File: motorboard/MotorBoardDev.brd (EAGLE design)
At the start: 86 x 80.5 mm, 70 parts, among them J1 Under Glow, J2 B2PS-VH(LF)(SN), J3 B2PS-VH(LF)(SN), J4 B2PS-VH(LF)(SN), Q1 SSM3J338R, Q2 SSM3J338R, Q3 SSM3J338R, Q4 STT4P3LLH6, U1 TXB0104DR, U2 9DoF IMU, U3 TXB0106PWR, U4 TLV70233DBVR, X1 C-GRID-05-15-91, X2 C-GRID-05-15-91, X3 MINI-USB_SHIELD5P4-32005-400, X4 C-GRID-02-70553, X5 SI-50170, X7 2510-, X8 2510-

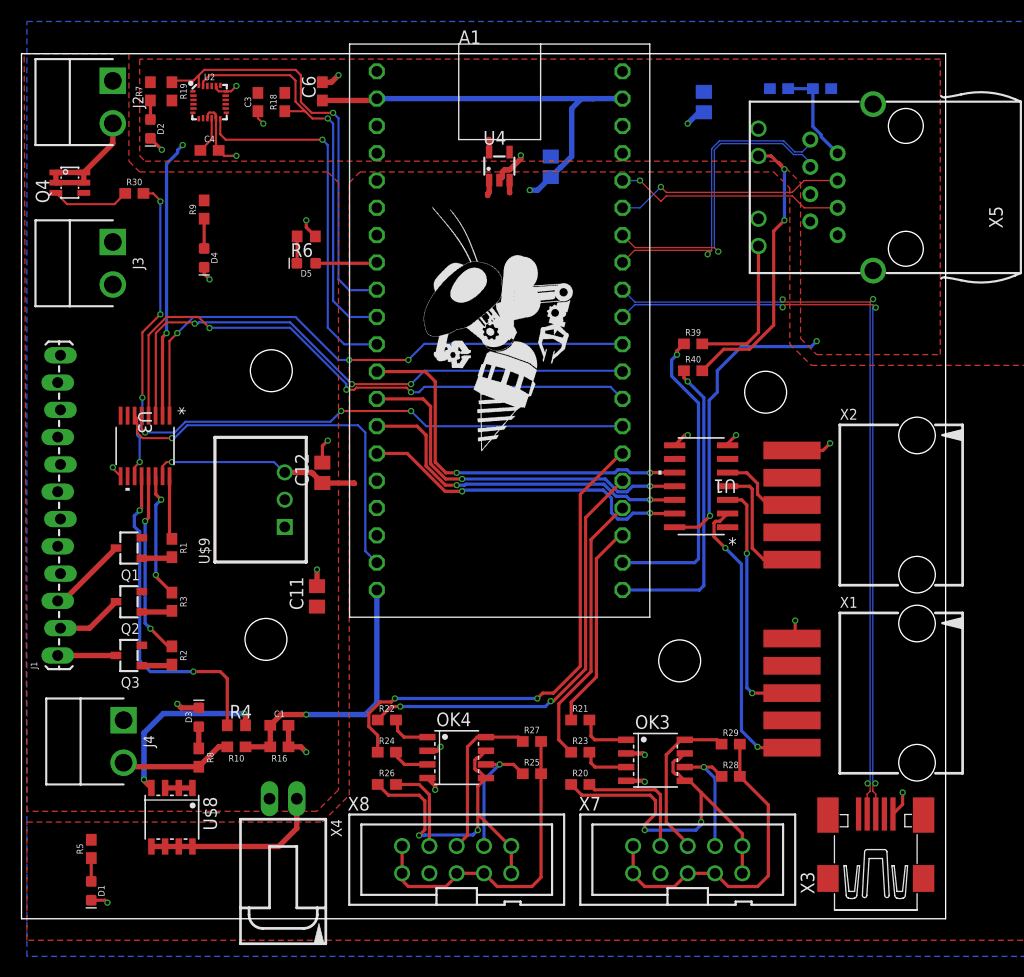
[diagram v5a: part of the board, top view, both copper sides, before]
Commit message: Differential and Silkscreen fixed
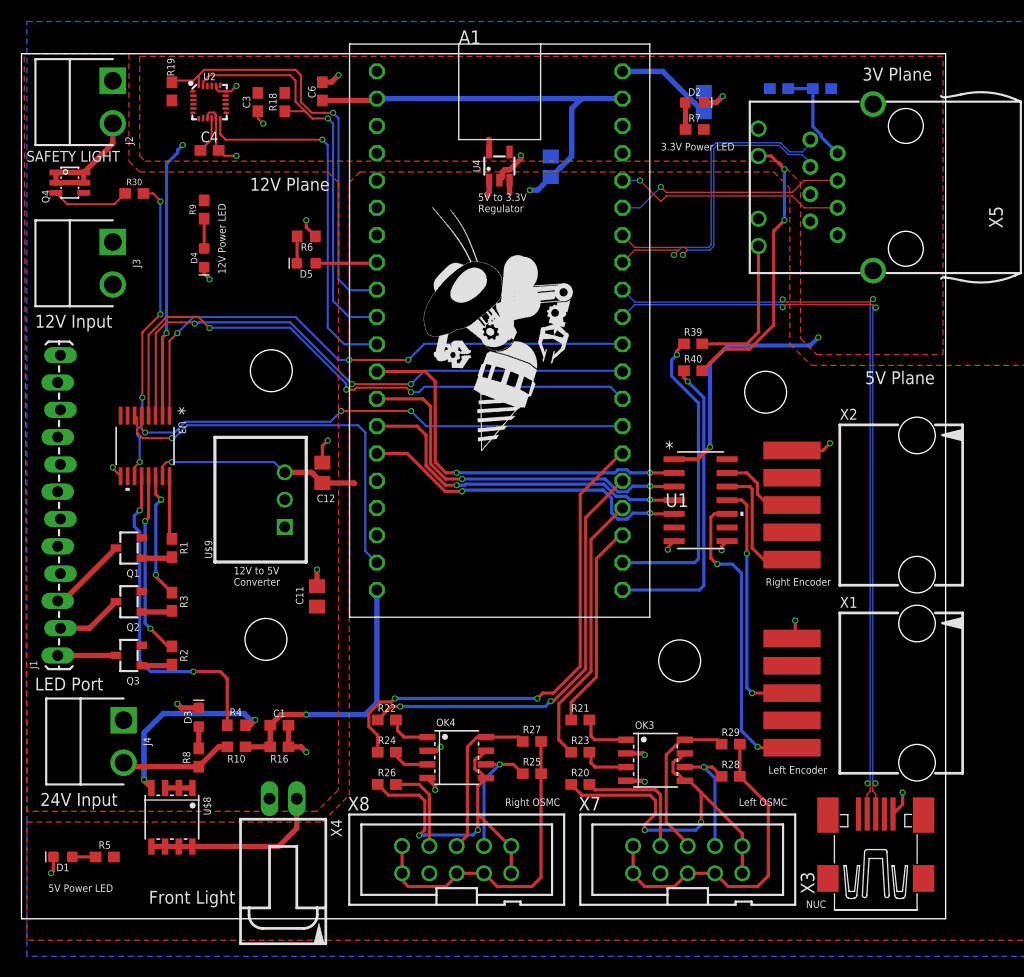
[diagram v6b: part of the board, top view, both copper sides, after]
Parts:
- moved R7 50.8 mm to (70.2, 73.5), turned to 0 degrees
- moved D2 50.7 mm to (70.2, 76.0), turned to 0 degrees
- moved D1 4.12 mm to (11.3, 5.76), turned to 180 degrees
- moved R5 1.46 mm to (15.2, 5.75), turned to 0 degrees
- moved U1 1.30 mm to (70.7, 39.0), turned to 0 degrees
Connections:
- net N$1 renamed SAFETY_HRD
- net N$10 renamed FRONT_HDR
- net N$12 renamed 12V_LED_R
- net N$17 renamed MBED_R_LED1
- net N$18 renamed MBED_R_LED2
- net N$19 renamed GREEN_R
- net N$2 renamed REGOUT_C
- net N$26 renamed RED_R
- net N$29 renamed R_OK3A
- net N$3 renamed INDI_LED_R
- net N$30 renamed R_OK4A
- net N$31 renamed R_OK4B
- net N$32 renamed R_OK3B
- net N$4 renamed BLUE_R
- net N$5 renamed 5V_LED_R
- net N$6 renamed 3V3_LED_R
- net N$7 renamed SAFETY_R
- net N$8 renamed FRONT_R
- net N$9 renamed 24V_LED_R
- net +3V3: now also U1.1; no longer U1.14
- net +5V: now also U1.14; no longer U1.1
- net LEA: now also U1.11; no longer U1.3
- net LEA3: now also U1.4; no longer U1.12
- net LEB: now also U1.10; no longer U1.2
- net LEB3: now also U1.5; no longer U1.13
- net REA: now also U1.13; no longer U1.5
- net REA3: now also U1.2; no longer U1.10
- net REB: now also U1.12; no longer U1.4
- net REB3: now also U1.3; no longer U1.11
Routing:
- net +3V3: track 66.3 -> 68.2 mm, vias 5 -> 4
- net LEB: track 27.4 -> 28.9 mm
- net FRONT_R: track 16.6 -> 17.9 mm
- net +5V: track 62.5 -> 61.4 mm
- net 3V3_LED_R: track 1.77 -> 2.51 mm
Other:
- board text added: "12V Input"
- board text added: "12V Plane"
- board text added: "12V Power LED"
- board text added: "12V to 5V Converter"
- board text added: "24V Input"
- board text added: "3.3V Power LED"
- board text added: "3V Plane"
- board text added: "5V Plane"
- board text added: "5V Power LED"
- board text added: "5V to 3.3V Regulator"
- board text added: "Front Light"
- board text added: "LED Port"
- board text added: "Left Encoder"
- board text added: "Left OSMC"
- board text added: "NUC"
- board text added: "Right Encoder"
- board text added: "Right OSMC"
- board text added: "SAFETY LIGHT"

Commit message: moved board
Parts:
- moved D2 7.50 mm to (62.6, 76.0)
- moved R7 7.50 mm to (62.6, 73.5)
- moved A1 7.50 mm to (44.5, 56.0)
- moved C1 7.50 mm to (24.0, 18.0)
- moved C11 7.50 mm to (27.5, 30.0)
- moved C12 7.50 mm to (28.0, 41.5)
- moved C13 7.50 mm to (49.3, 70.0)
- moved C14 7.50 mm to (63.5, 76.0)
- moved C2 7.50 mm to (74.5, 77.2)
- moved C3 7.50 mm to (22.0, 76.0)
- moved C4 7.50 mm to (17.5, 71.5)
- moved C5 7.50 mm to (70.5, 77.2)
- moved C6 7.50 mm to (28.0, 77.0)
- moved D1 7.50 mm to (3.85, 5.76)
- moved D3 7.50 mm to (16.5, 18.8)
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
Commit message: changed front light to flood light
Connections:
- net RD+ renamed RD_P
- net RD- renamed RD_N
- net GND: now also U3.8
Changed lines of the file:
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@@
 <wire x1="64.65" y1="75.95" x2="65.25" y2="76.55" width="0.5" layer="1"/>
 <via x="65.25" y="76.55" extent="1-16" drill="0.35"/>
+<contactref element="U3" pad="8"/>
+<wire x1="75.35" y1="77.25" x2="79.25" y2="75.812" width="0" layer="19" extent="16-16"/>
+<wire x1="69.65" y1="77.25" x2="75.35" y2="77.25" width="0" layer="19" extent="16-16"/>
+<wire x1="68.582" y1="73.526" x2="69.65" y2="77.25" width="0" layer="19" extent="16-16"/>
+<wire x1="65.25" y1="76.55" x2="69.65" y2="77.25" width="0" layer="19" extent="16-16"/>
+<wire x1="63.5" y1="76.95" x2="63.527" y2="75.95" width="0" layer="19" extent="1-16"/>
+<wire x1="68.582" y1="65.144" x2="68.582" y2="73.526" width="0" layer="19" extent="1-1"/>
+<wire x1="79.25" y1="60.318" x2="68.582" y2="65.144" width="0" layer="19" extent="1-1"/>
+<wire x1="49.26" y1="70.93" x2="63.527" y2="75.95" width="0" layer="19" extent="1-16"/>
+<wire x1="46.47" y1="71.04" x2="49.26" y2="70.93" width="0" layer="19" extent="16-16"/>
+<wire x1="33.07" y1="78.86" x2="44.745" y2="69.48933125" width="0" layer="19" extent="1-1"/>
+<wire x1="29.5" y1="78.5" x2="33.07" y2="78.86" width="0" layer="19" extent="1-1"/>
+<wire x1="22" y1="75.15" x2="28" y2="77.85" width="0" layer="19" extent="1-1"/>
+<wire x1="20" y1="77.5" x2="22" y2="75.15" width="0" layer="19" extent="1-1"/>
+<wire x1="17.9182" y1="75.025" x2="18.3618" y2="77" width="0" layer="19" extent="1-1"/>
+<wire x1="26.5" y1="65" x2="20" y2="71" width="0" layer="19" extent="1-1"/>
+<wire x1="8.5" y1="77.98" x2="17.35" y2="74.8932" width="0" layer="19" extent="1-1"/>
+<wire x1="17" y1="60.623" x2="26.5" y2="64.35" width="0" layer="19" extent="1-1"/>
+<wire x1="8.5" y1="62.98" x2="17" y2="60.623" width="0" layer="19" extent="1-1"/>
+<wire x1="3.627" y1="52.44" x2="8.5" y2="62.98" width="0" layer="19" extent="1-1"/>
+<wire x1="3.373" y1="49.9" x2="3.627" y2="52.44" width="0" layer="19" extent="1-1"/>
+<wire x1="3.627" y1="47.36" x2="3.373" y2="49.9" width="0" layer="19" extent="1-1"/>
+<wire x1="9.225" y1="46.8194" x2="3.627" y2="47.36" width="0" layer="19" extent="1-1"/>
+<wire x1="8.5" y1="42" x2="9.225" y2="46.8194" width="0" layer="19" extent="1-1"/>
+<wire x1="3.627" y1="37.2" x2="8.5" y2="41.9056" width="0" layer="19" extent="1-1"/>
+<wire x1="3.373" y1="34.66" x2="3.627" y2="37.2" width="0" layer="19" extent="1-1"/>
+<wire x1="3.627" y1="32.12" x2="3.373" y2="34.66" width="0" layer="19" extent="1-1"/>
+<wire x1="9.5" y1="18.48" x2="3.627" y2="32.12" width="0" layer="19" extent="1-1"/>
+<wire x1="14.5" y1="20" x2="9.5" y2="18.48" width="0" layer="19" extent="1-1"/>
+<wire x1="24.85" y1="18" x2="16.5" y2="19.627" width="0" layer="19" extent="1-1"/>
+<wire x1="23.08" y1="11.17" x2="24.85" y2="16" width="0" layer="19" extent="1-1"/>
+<wire x1="37.7766" y1="15.635" x2="26.5" y2="15.5" width="0" layer="19" extent="1-1"/>
+<wire x1="37.7766" y1="13.095" x2="37.7766" y2="15.635" width="0" layer="19" extent="1-1"/>
+<wire x1="27.5" y1="30.95" x2="24.85" y2="18" width="0" layer="19" extent="1-1"/>
+<wire x1="24.5" y1="39" x2="27.5" y2="32.5" width="0" layer="19" extent="1-1"/>
+<wire x1="28" y1="42.45" x2="24.5" y2="39" width="0" layer="19" extent="1-1"/>
+<wire x1="2.973" y1="5.76" x2="9.5" y2="18.48" width="0" layer="19" extent="1-1"/>
+<wire x1="75.25" y1="44.25" x2="79.25" y2="60.318" width="0" layer="19" extent="1-1"/>
+<wire x1="65.6638" y1="35.14" x2="71.705" y2="43.58" width="0" layer="19" extent="1-1"/>
+<wire x1="60.7362" y1="35.14" x2="65.15" y2="34.6262" width="0" layer="19" extent="1-1"/>
+<wire x1="72" y1="27.75" x2="65.15" y2="34.3" width="0" layer="19" extent="1-1"/>
+<wire x1="56.2766" y1="15.385" x2="39" y2="16" width="0" layer="19" extent="1-1"/>
+<wire x1="57.905" y1="12.845" x2="58" y2="15.25" width="0" layer="19" extent="1-1"/>
+<wire x1="82" y1="11.75" x2="71.705" y2="26.08" width="0" layer="19" extent="1-1"/>
 </signal>
 <signal name="SDA">
@@
 <wire x1="17" y1="65.15" x2="17" y2="62.377" width="0.3" layer="1"/>
 </signal>
-<signal name="RD-">
+<signal name="RD_N">
 <contactref element="A1" pad="36"/>
 <contactref element="X5" pad="6"/>
@@
 <wire x1="25.65" y1="61.027" x2="25.65" y2="63.5" width="0.3" layer="1"/>
 </signal>
-<signal name="RD+">
+<signal name="RD_P">
 <contactref element="A1" pad="35"/>
 <contactref element="X5" pad="4"/>
